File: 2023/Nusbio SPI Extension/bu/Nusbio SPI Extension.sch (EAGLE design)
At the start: 7 parts

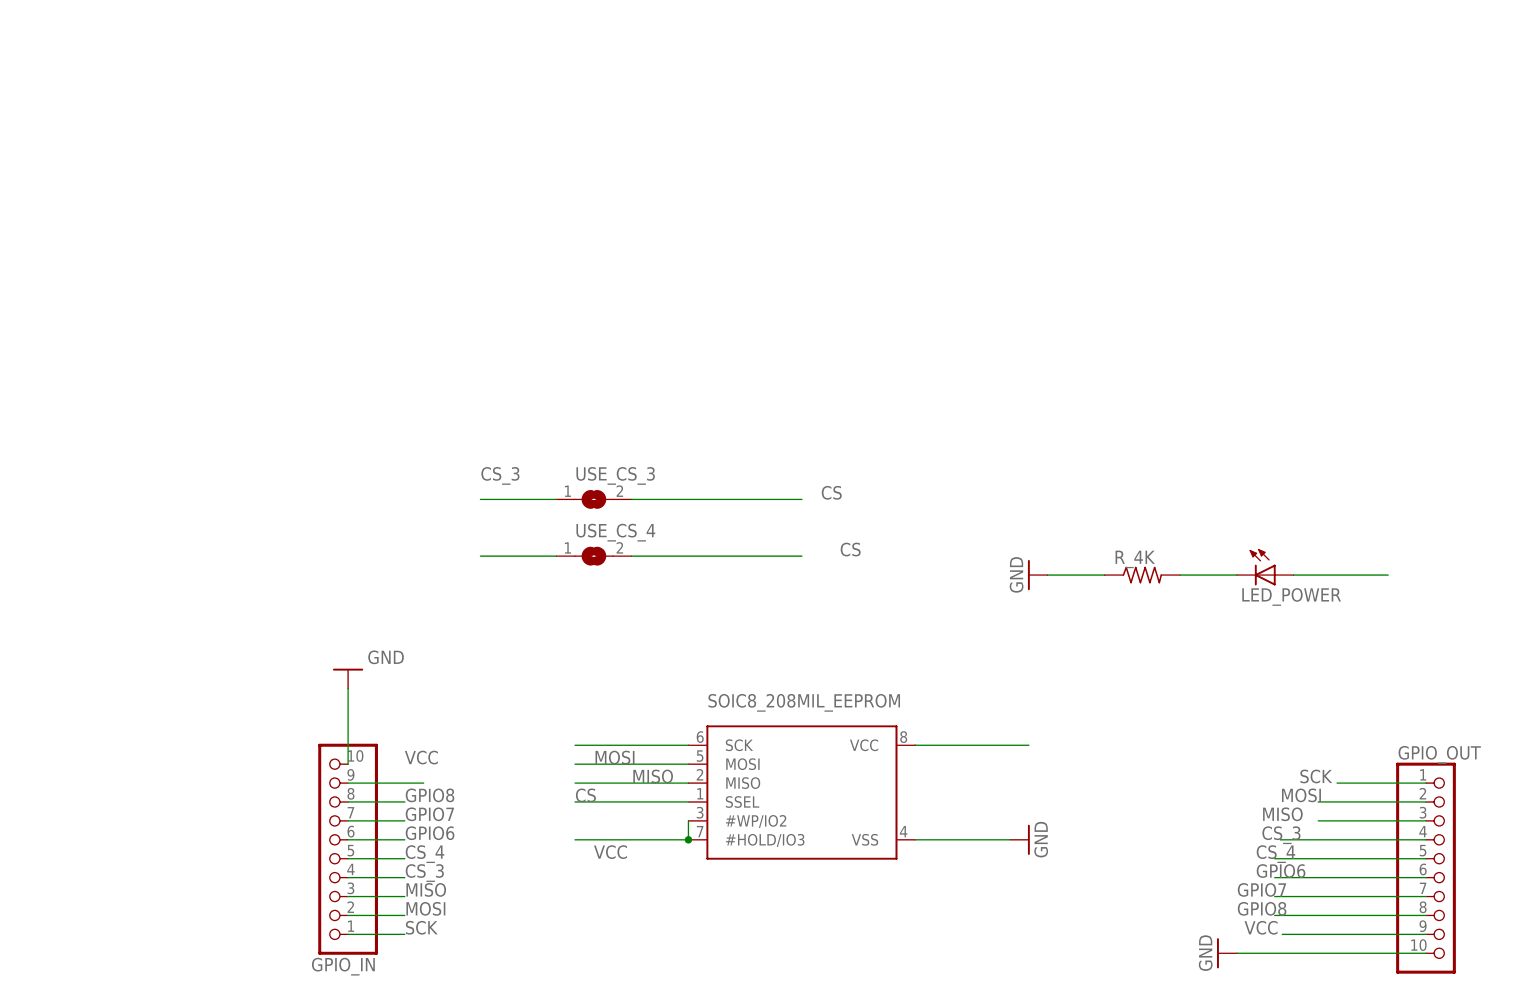
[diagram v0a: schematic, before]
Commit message: SPI Extension
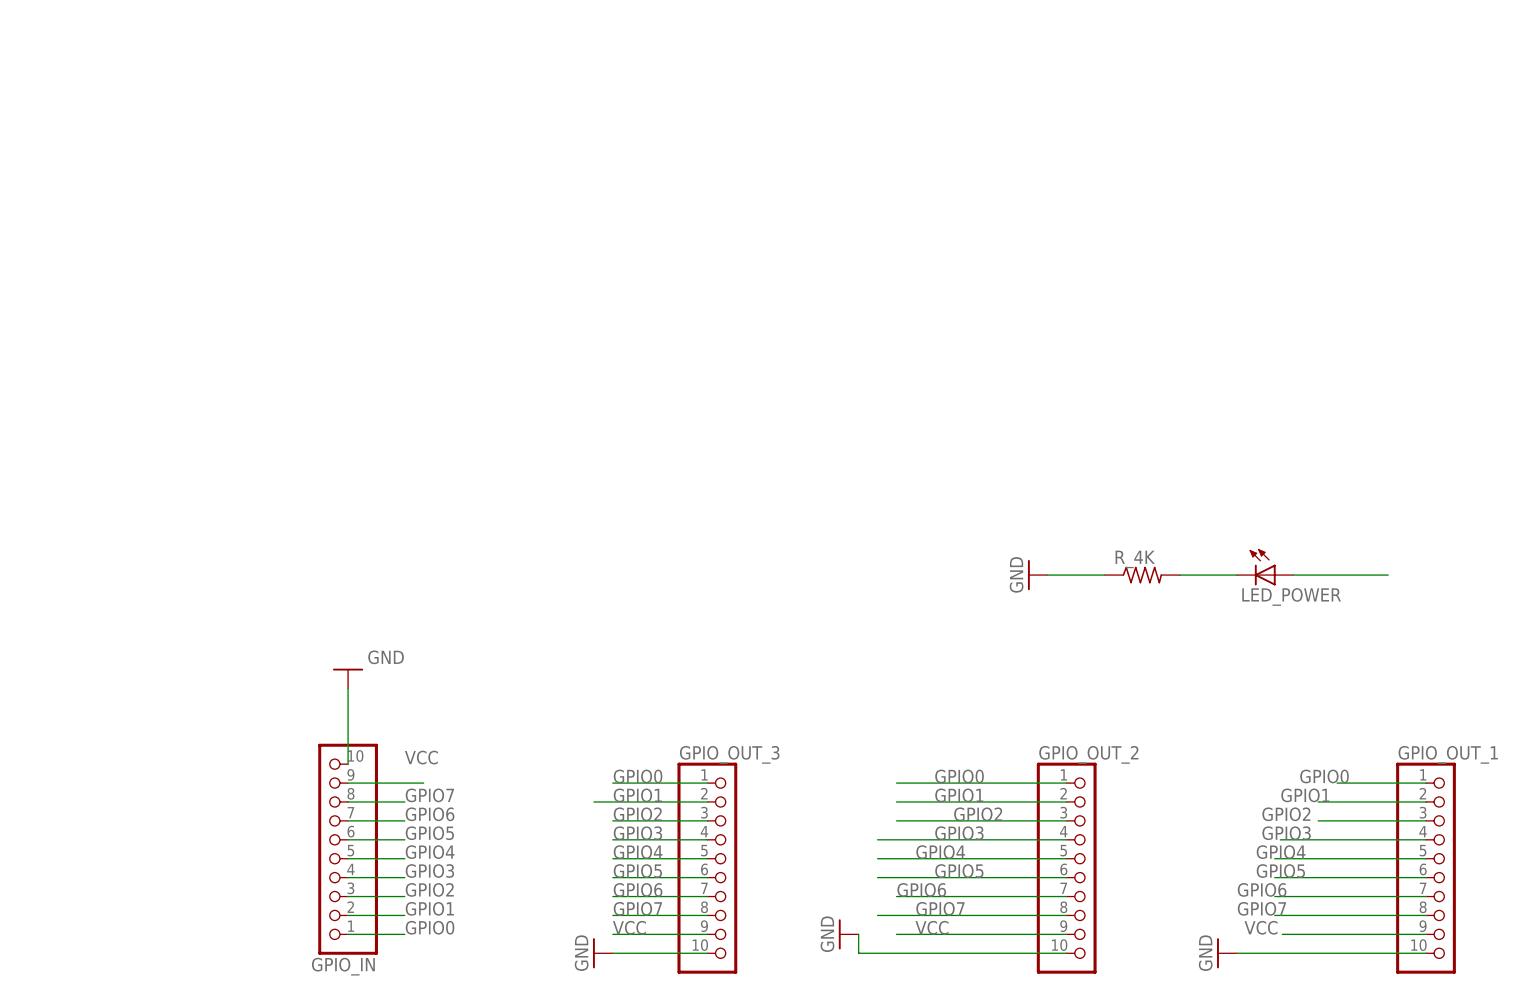
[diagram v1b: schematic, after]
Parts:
- removed SOIC8_208MIL_EEPROM: (no value), microbuilder:SPIFLASH_SOIC8208MIL
- removed USE_CS_3, USE_CS_4: (no value), microbuilder:SOLDERJUMPERREFLOW
- added GPIO_OUT_2, GPIO_OUT_3: PINHD-1X10, adafruit:PINHD-1X10
- renumbered GPIO_OUT to GPIO_OUT_1
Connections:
- removed net CS: SOIC8_208MIL_EEPROM.SSEL, USE_CS_3.2, USE_CS_4.2
- removed net CS_3: GPIO_IN.4, GPIO_OUT_1.4, USE_CS_3.1
- removed net CS_4: GPIO_IN.5, GPIO_OUT_1.5, USE_CS_4.1
- removed net GPIO8: GPIO_IN.8, GPIO_OUT_1.8
- removed net MISO: GPIO_IN.3, GPIO_OUT_1.3, SOIC8_208MIL_EEPROM.MISO
- removed net MOSI: GPIO_IN.2, GPIO_OUT_1.2, SOIC8_208MIL_EEPROM.MOSI
- removed net SCK: GPIO_IN.1, GPIO_OUT_1.1, SOIC8_208MIL_EEPROM.SCK
- new net GPIO0: GPIO_IN.1, GPIO_OUT_1.1, GPIO_OUT_2.1, GPIO_OUT_3.1
- new net GPIO1: GPIO_IN.2, GPIO_OUT_1.2, GPIO_OUT_2.2, GPIO_OUT_3.2
- new net GPIO2: GPIO_IN.3, GPIO_OUT_1.3, GPIO_OUT_2.3, GPIO_OUT_3.3
- new net GPIO3: GPIO_IN.4, GPIO_OUT_1.4, GPIO_OUT_2.4, GPIO_OUT_3.4
- new net GPIO4: GPIO_IN.5, GPIO_OUT_1.5, GPIO_OUT_2.5, GPIO_OUT_3.5
- new net GPIO5: GPIO_IN.6, GPIO_OUT_1.6, GPIO_OUT_2.6, GPIO_OUT_3.6
- net GND: now also GPIO_OUT_2.10, GPIO_OUT_3.10; no longer SOIC8_208MIL_EEPROM.VSS
- net GPIO6: now also GPIO_IN.7, GPIO_OUT_1.7, GPIO_OUT_2.7, GPIO_OUT_3.7; no longer GPIO_IN.6, GPIO_OUT_1.6
- net GPIO7: now also GPIO_IN.8, GPIO_OUT_1.8, GPIO_OUT_2.8, GPIO_OUT_3.8; no longer GPIO_IN.7, GPIO_OUT_1.7
- net VCC: now also GPIO_OUT_2.9, GPIO_OUT_3.9; no longer SOIC8_208MIL_EEPROM.#HOLD/IO3, SOIC8_208MIL_EEPROM.#WP/IO2, SOIC8_208MIL_EEPROM.VCC

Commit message: Nusbio v2 pcb and SPIExtension v 1 2023/05
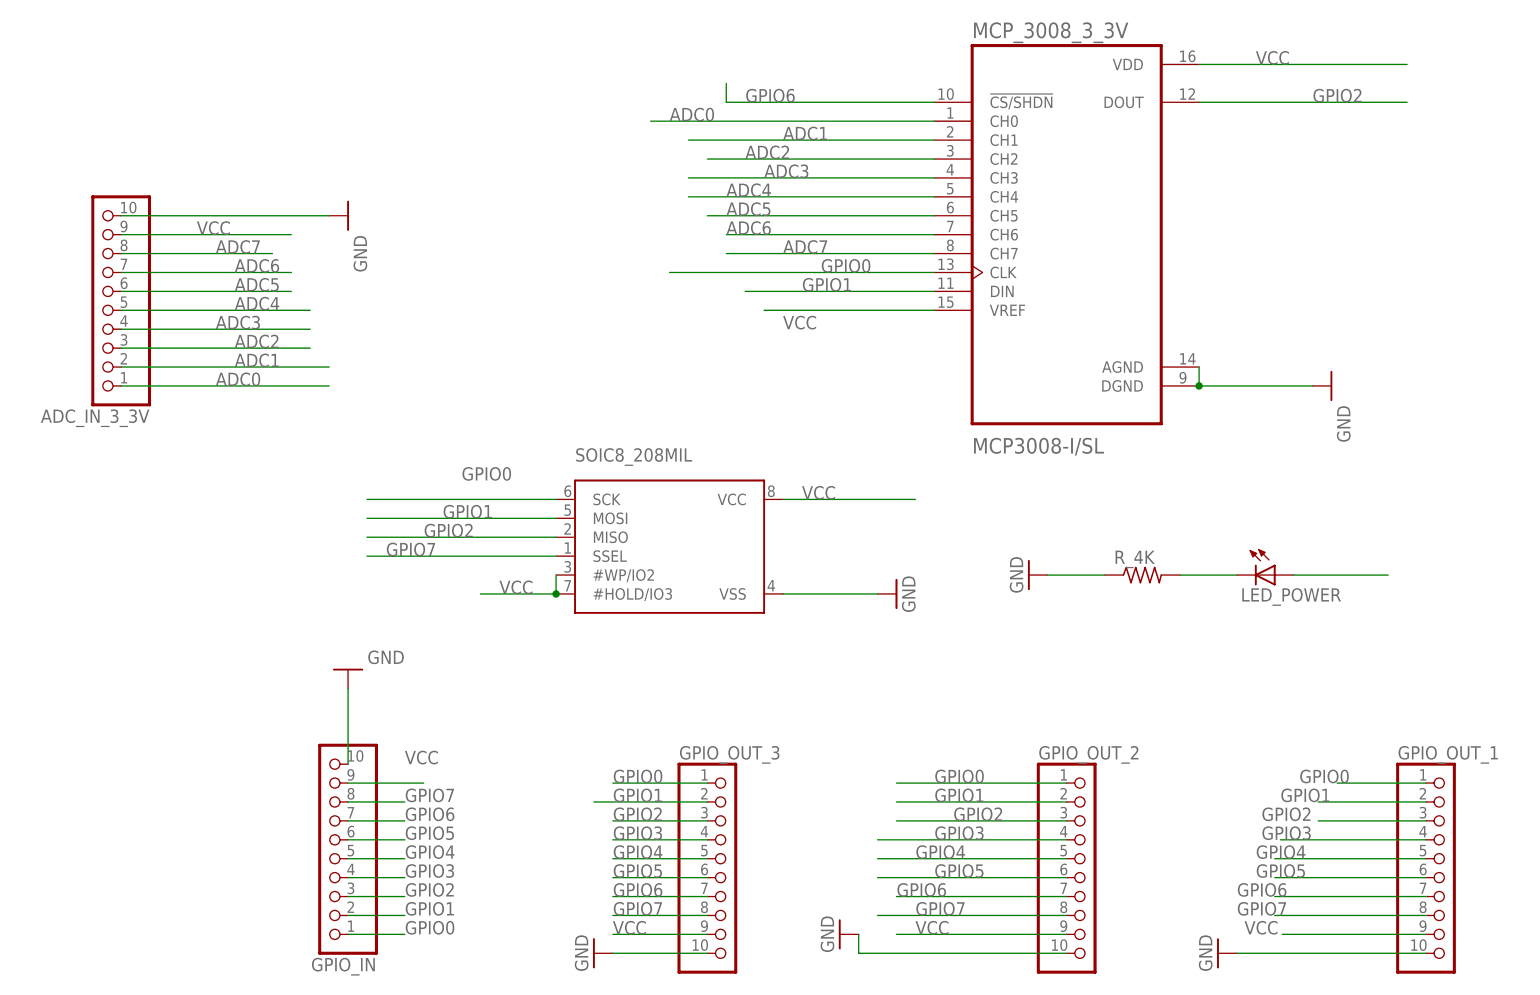
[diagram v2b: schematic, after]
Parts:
- added ADC_IN_3_3V: PINHD-1X10, adafruit:PINHD-1X10
- added MCP_3008_3_3V: MCP3008-I/SL, MCP3008-I_SL:MCP3008-I/SL
- added SOIC8_208MIL: (no value), microbuilder:SPIFLASH_SOIC8208MIL
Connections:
- new net ADC0: ADC_IN_3_3V.1, MCP_3008_3_3V.CH0
- new net ADC1: ADC_IN_3_3V.2, MCP_3008_3_3V.CH1
- new net ADC2: ADC_IN_3_3V.3, MCP_3008_3_3V.CH2
- new net ADC3: ADC_IN_3_3V.4, MCP_3008_3_3V.CH3
- new net ADC4: ADC_IN_3_3V.5, MCP_3008_3_3V.CH4
- new net ADC5: ADC_IN_3_3V.6, MCP_3008_3_3V.CH5
- new net ADC6: ADC_IN_3_3V.7, MCP_3008_3_3V.CH6
- new net ADC7: ADC_IN_3_3V.8, MCP_3008_3_3V.CH7
- net GND: now also ADC_IN_3_3V.10, MCP_3008_3_3V.AGND, MCP_3008_3_3V.DGND, SOIC8_208MIL.VSS
- net GPIO0: now also MCP_3008_3_3V.CLK, SOIC8_208MIL.SCK
- net GPIO1: now also MCP_3008_3_3V.DIN, SOIC8_208MIL.MOSI
- net GPIO2: now also MCP_3008_3_3V.DOUT, SOIC8_208MIL.MISO
- net GPIO6: now also MCP_3008_3_3V.!CS/SHDN
- net GPIO7: now also SOIC8_208MIL.SSEL
- net VCC: now also ADC_IN_3_3V.9, MCP_3008_3_3V.VDD, MCP_3008_3_3V.VREF, SOIC8_208MIL.#HOLD/IO3, SOIC8_208MIL.#WP/IO2, SOIC8_208MIL.VCC
